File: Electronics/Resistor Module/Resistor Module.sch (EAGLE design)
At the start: 110 parts, among them IC1 74HC595D, IC2 74HC595D, IC3 74HC595D, IC4 74HC595D

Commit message: Updated schematic for full range module. 1/4 layout done.
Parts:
- removed $1_75_$: 25AA010A, Resistor Module Library:25AA010A
- removed JP3: (no value), Resistor Module Library:M03X2SMT-M0.1
- removed JP4: M10PASSTHROUGH, Resistor Module Library:M10PASSTHROUGH
- removed R33, R34, R35, R36, R37, R38, R39, R40: 2k, Resistor Module Library:RESISTOR0603-RES
- added R100: 10, Resistor Module Library:RESISTOR1206
- added R120: 1k, Resistor Module Library:RESISTOR1206
- added R160: 10k, Resistor Module Library:RESISTOR1206
- added R200: 100k, Resistor Module Library:RESISTOR1206
- added R240: 1M, Resistor Module Library:RESISTOR1206
- added R280: 10M, Resistor Module Library:RESISTOR1206
- added R320: 100M, Resistor Module Library:RESISTOR1206
- added R65, R66, R67, R68, R69, R70, R71, R72: 2k, Resistor Module Library:RESISTOR0603-RES
- added R73: 10k, Resistor Module Library:RESISTOR0603-RES
- added R80: 100, Resistor Module Library:RESISTOR1206
- added S29, S30, S31, S32: CPC1002N, Resistor Module Library:CPC1002N
- added U5: 25AA010A, Resistor Module Library:25AA010A
- JP2: value (none) -> M10PASSTHROUGH; device Resistor Module Library:M03X2969973-3 -> Resistor Module Library:M10PASSTHROUGH
- R25: value 10 -> 1M
- R26: value 100 -> 2M
- R27: value 1k -> 2M
- R28: value 10k -> 10M
- R29: value 100k -> 10M
- R30: value 1M -> 20M
- R31: value 2k -> 20M; device Resistor Module Library:RESISTOR0603-RES -> Resistor Module Library:RESISTOR1206
- R32: value 2k -> 100M; device Resistor Module Library:RESISTOR0603-RES -> Resistor Module Library:RESISTOR1206
- R59: value 10k -> 2k
- R60: value 1M -> 2k; device Resistor Module Library:RESISTOR1206 -> Resistor Module Library:RESISTOR0603-RES
- R61, R62: value 2M -> 2k; device Resistor Module Library:RESISTOR1206 -> Resistor Module Library:RESISTOR0603-RES
- R63, R64: value 10M -> 2k; device Resistor Module Library:RESISTOR1206 -> Resistor Module Library:RESISTOR0603-RES
- renumbered IC1 to U1, IC2 to U2, IC3 to U3, IC4 to U4
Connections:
- removed net N$40: R12.1, R13.2, R27.1, S12.DC-, S13.DC+
- removed net N$43: R16.1, R17.2, R28.1, S16.DC-, S17.DC+
- removed net N$9: R26.1, R8.1, R9.2, S8.DC-, S9.DC+
- removed net RELAY_POST_SHORT: R37.2, R51.2
- removed net RELAY_PRE_SHORT: R38.2, R52.2
- removed net R_DOWNSTREAM_IN: JP2.1
- removed net R_DOWNSTREAM_OUT: JP3.1
- removed net R_UPSTREAM: JP2.6, JP3.2
- removed net SERIAL_OUT: JP3.6
- new net N$53: R28.1, R280.1, R29.2, S28.DC-, S29.DC+
- new net N$58: R29.1, R30.2, S29.DC-, S30.DC+
- new net N$59: R30.1, R31.2, S30.DC-, S31.DC+
- new net N$60: R31.1, R32.2, R320.2, S31.DC-, S32.DC+
- new net N$61: R49.1, U2A.QA
- new net N$62: R57.1, U3A.QA
- new net N$64: R65.1, U4A.QA
- new net R120: R12.1, R120.1, R13.2, S12.DC-, S13.DC+
- new net R160: R16.1, R160.1, R17.2, S16.DC-, S17.DC+
- new net R80: R8.1, R80.1, R9.2, S8.DC-, S9.DC+
- new net RELAY_R29: R69.2, S29.C+
- new net RELAY_R30: R70.2, S30.C+
- new net RELAY_R31: R71.2, S31.C+
- new net RELAY_R32: R72.2, S32.C+
- new net R_OUT: JP2.2, R32.1, R320.1, S32.DC-
- net 5V: now also R73.2, U5.VDD; no longer $1_75_$.VDD, R59.2
- net 5V_2: now also JP2.6; no longer JP4.6
- net EEPROM_CS_L: now also JP1.1, R73.1, U5.CS; no longer $1_75_$.CS, R59.1, U1A.QA, U3A.QA
- net EEPROM_MISO: now also U5.SO; no longer $1_75_$.SO
- net EEPROM_MOSI: now also U5.SI; no longer $1_75_$.SI
- net EEPROM_SCK: now also U5.SCK; no longer $1_75_$.SCK
- net GND: now also S29.C-, S30.C-, S31.C-, S32.C-, U5.VSS; no longer $1_75_$.VSS
- net GND_2: now also JP2.5; no longer JP4.5
- net N$1: now also R48.1; no longer R37.1
- net N$12: now also R46.1; no longer R35.1
- net N$13: now also R45.1; no longer R34.1
- net N$14: now also R44.1; no longer R33.1
- net N$15: now also R120.2; no longer R27.2
- net N$16: now also R43.1; no longer R32.1
- net N$17: now also R42.1; no longer R31.1
- net N$18: now also R50.1; no longer R38.1
- net N$19: now also R51.1; no longer R39.1
- net N$2: now also R47.1; no longer R36.1
- net N$20: now also R52.1; no longer R40.1
- net N$21: now also R53.1; no longer R41.1
- net N$22: now also R54.1; no longer R42.1
- net N$23: now also R55.1; no longer R43.1
- net N$24: now also R56.1; no longer R44.1
- net N$26: now also R64.1; no longer R51.1
- net N$27: now also R63.1; no longer R50.1
- net N$28: now also R62.1; no longer R49.1
- net N$29: now also R61.1; no longer R48.1
- net N$30: now also R60.1; no longer R47.1
- net N$31: now also R59.1; no longer R46.1
- net N$32: now also R58.1; no longer R45.1
- net N$33: now also R66.1; no longer R52.1
- net N$34: now also R67.1; no longer R53.1
- net N$35: now also R68.1; no longer R54.1
- net N$36: now also R69.1; no longer R55.1
- net N$37: now also R70.1; no longer R56.1
- net N$38: now also R71.1; no longer R57.1
- net N$39: now also R72.1; no longer R58.1
- net N$4: now also R100.2; no longer R25.2
- net N$42: now also R160.2; no longer R28.2
- net N$46: now also R200.2; no longer R29.2
- net N$47: now also R200.1; no longer R29.1
- net N$5: now also R100.1; no longer R25.1
- net N$50: now also R240.2; no longer R30.2
- net N$52: now also R240.1, R25.2; no longer R30.1, R60.2
- net N$54: now also R25.1, R26.2; no longer R60.1, R61.2
- net N$55: now also R26.1, R27.2; no longer R61.1, R62.2
- net N$56: now also R27.1, R28.2, R280.2; no longer R62.1, R63.2, R64.2
- net N$57: now also R41.1, U1A.QA; no longer R63.1, R64.1, S28.DC-
- net N$8: now also R80.2; no longer R26.2
- net RELAY_R1: now also R41.2; no longer R36.2, R50.2
- net RELAY_R10: now also R50.2; no longer R41.2, R55.2
- net RELAY_R11: now also R51.2; no longer R40.2, R54.2
- net RELAY_R12: now also R52.2; no longer R39.2, R53.2
- net RELAY_R13: now also R53.2
- net RELAY_R14: now also R54.2
- net RELAY_R15: now also R55.2
- net RELAY_R16: now also R56.2
- net RELAY_R17: now also R57.2
- net RELAY_R18: now also R58.2
- net RELAY_R19: now also R59.2
- net RELAY_R2: now also R42.2; no longer R35.2, R49.2
- net RELAY_R20: now also R60.2
- net RELAY_R21: now also R61.2
- net RELAY_R22: now also R62.2
- net RELAY_R23: now also R63.2
- net RELAY_R24: now also R64.2
- net RELAY_R25: now also R65.2
- net RELAY_R26: now also R66.2
- net RELAY_R27: now also R67.2
- net RELAY_R28: now also R68.2
- net RELAY_R3: now also R43.2; no longer R34.2, R48.2
- net RELAY_R4: now also R44.2; no longer R33.2, R47.2
- net RELAY_R5: now also R45.2; no longer R32.2, R46.2
- net RELAY_R6: now also R46.2; no longer R31.2, R45.2
- net RELAY_R7: now also R47.2; no longer R44.2, R58.2
- net RELAY_R8: now also R48.2; no longer R43.2, R57.2
- net RELAY_R9: now also R49.2; no longer R42.2, R56.2
- net R_IN: now also JP2.1
- net SERIAL_CLK: now also JP1.8, U2A.SCK; no longer JP1.9, U3A.SCK
- net SERIAL_CLK_2: now also JP2.8, U3A.SCK; no longer JP4.9, U2A.SCK
- net SERIAL_IN: now also JP2.4; no longer JP2.2
- net SERIAL_LATCH: now also JP1.9, U2A.RCK; no longer JP1.8, U3A.RCK
- net SERIAL_LATCH_2: now also JP2.9, U3A.RCK; no longer JP4.8, U2A.RCK
- net SERIAL_MR_L: now also JP1.7, U2A.SCL; no longer JP1.10, U3A.SCL
- net SERIAL_MR_L_2: now also JP2.7, U3A.SCL; no longer JP4.10, U2A.SCL
- net SERIAL_OE_L: now also JP1.10, U2A.G; no longer JP1.7, U3A.G
- net SERIAL_OE_L_2: now also JP2.10, U3A.G; no longer JP4.7, U2A.G
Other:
- note removed: "BOTTOM"
- note removed: "TOP"
- moved on the sheet: C5, JP2, R25, R26, R27, R28, R29, R30, R41, R42, R43, R44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

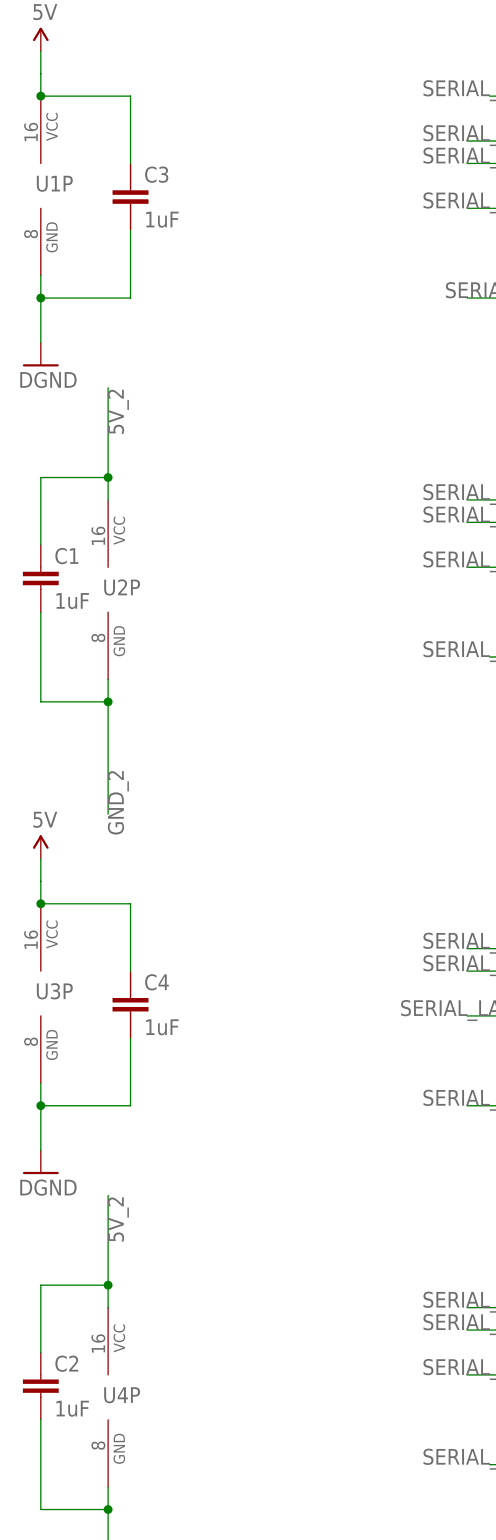
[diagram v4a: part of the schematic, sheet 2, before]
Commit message: Placed all relays and critical resistors.
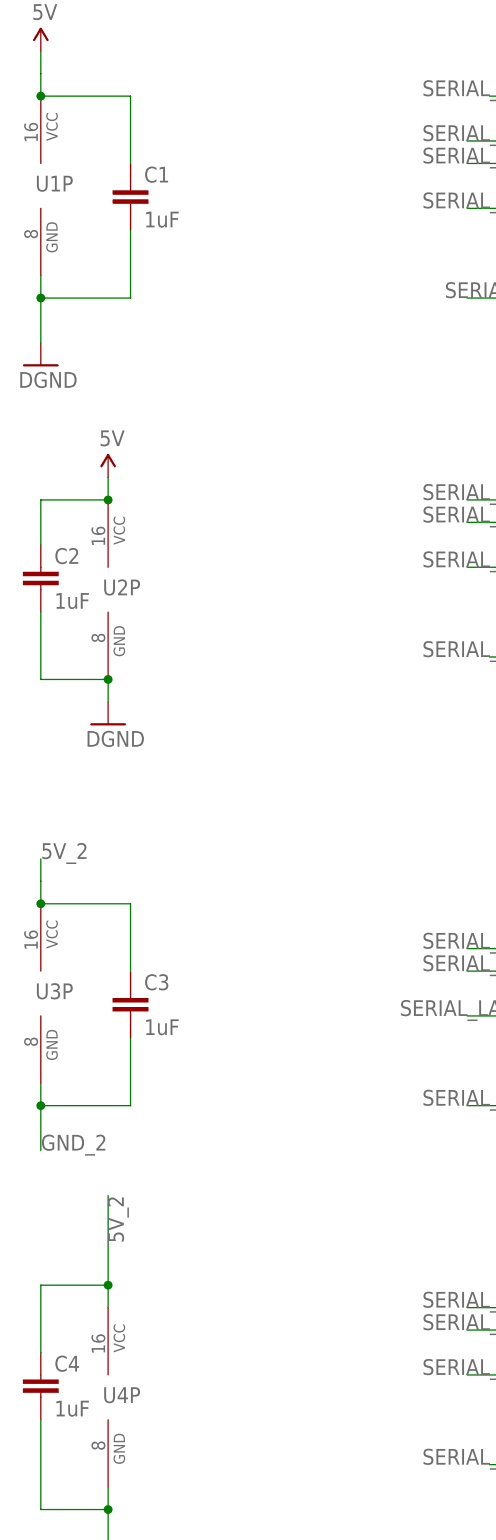
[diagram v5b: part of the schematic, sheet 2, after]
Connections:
- net 5V: now also C1.1, C2.1, U2P.VCC; no longer C3.1, C4.1, U3P.VCC
- net 5V_2: now also C3.1, C4.1, U3P.VCC; no longer C1.1, C2.1, U2P.VCC
- net GND: now also C1.2, C2.2, U2P.GND; no longer C3.2, C4.2, U3P.GND
- net GND_2: now also C3.2, C4.2, U3P.GND; no longer C1.2, C2.2, U2P.GND
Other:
- moved on the sheet: C1, C2, C3, C4
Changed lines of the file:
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@@
 <part name="SUPPLY6" library="Resistor Module Library" deviceset="5V" device=""/>
 <part name="GND19" library="Resistor Module Library" deviceset="DGND" device=""/>
-<part name="C3" library="Resistor Module Library" deviceset="CAP" device="0603-CAP" value="1uF"/>
 <part name="C1" library="Resistor Module Library" deviceset="CAP" device="0603-CAP" value="1uF"/>
+<part name="C2" library="Resistor Module Library" deviceset="CAP" device="0603-CAP" value="1uF"/>
 <part name="C5" library="Resistor Module Library" deviceset="CAP" device="0603-CAP" value="1uF"/>
 <part name="GND2" library="Resistor Module Library" deviceset="DGND" device=""/>
 <part name="U3" library="Resistor Module Library" deviceset="74*595" device="D" technology="HC" value="74HC595D"/>
 <part name="U4" library="Resistor Module Library" deviceset="74*595" device="D" technology="HC" value="74HC595D"/>
-<part name="SUPPLY2" library="Resistor Module Library" deviceset="5V" device=""/>
-<part name="GND9" library="Resistor Module Library" deviceset="DGND" device=""/>
 <part name="R66" library="Resistor Module Library" deviceset="RESISTOR" device="0603-RES" value="2k"/>
 <part name="R63" library="Resistor Module Library" deviceset="RESISTOR" device="0603-RES" value="2k"/>
@@
 <part name="R67" library="Resistor Module Library" deviceset="RESISTOR" device="0603-RES" value="2k"/>
 <part name="R64" library="Resistor Module Library" deviceset="RESISTOR" device="0603-RES" value="2k"/>
+<part name="C3" library="Resistor Module Library" deviceset="CAP" device="0603-CAP" value="1uF"/>
 <part name="C4" library="Resistor Module Library" deviceset="CAP" device="0603-CAP" value="1uF"/>
-<part name="C2" library="Resistor Module Library" deviceset="CAP" device="0603-CAP" value="1uF"/>
 <part name="GND10" library="Resistor Module Library" deviceset="DGND" device=""/>
 <part name="GND11" library="Resistor Module Library" deviceset="DGND" device=""/>
@@
 <part name="R65" library="Resistor Module Library" deviceset="RESISTOR" device="0603-RES" value="2k"/>
 <part name="R57" library="Resistor Module Library" deviceset="RESISTOR" device="0603-RES" value="2k"/>
+<part name="GND9" library="Resistor Module Library" deviceset="DGND" device=""/>
+<part name="SUPPLY2" library="Resistor Module Library" deviceset="5V" device=""/>
 </parts>
 <sheets>
@@
 </instance>
 <instance part="SUPPLY4" gate="G$1" x="35.56" y="-96.52"/>
-<instance part="C3" gate="G$1" x="-66.04" y="71.12"/>
-<instance part="C1" gate="G$1" x="-76.2" y="27.94"/>
+<instance part="C1" gate="G$1" x="-66.04" y="71.12"/>
+<instance part="C2" gate="G$1" x="-76.2" y="27.94"/>
 <instance part="C5" gate="G$1" x="0" y="-104.14" rot="R90"/>
 <instance part="GND2" gate="G$1" x="-15.24" y="-109.22"/>
@@
 <instance part="U3" gate="P" x="-76.2" y="-17.78"/>
 <instance part="U4" gate="P" x="-68.58" y="-63.5"/>
-<instance part="SUPPLY2" gate="G$1" x="-76.2" y="-2.54"/>
-<instance part="GND9" gate="G$1" x="-76.2" y="-38.1"/>
 <instance part="R66" gate="G$1" x="20.32" y="-50.8" smashed="yes">
 <attribute name="NAME" x="11.43" y="-50.5714" size="1.778" layer="95"/>
@@
 <attribute name="VALUE" x="25.4" y="-24.892" size="1.778" layer="96"/>
 </instance>
-<instance part="C4" gate="G$1" x="-66.04" y="-20.32"/>
-<instance part="C2" gate="G$1" x="-76.2" y="-63.5"/>
+<instance part="C3" gate="G$1" x="-66.04" y="-20.32"/>
+<instance part="C4" gate="G$1" x="-76.2" y="-63.5"/>
 <instance part="R41" gate="G$1" x="20.32" y="83.82" smashed="yes">
 <attribute name="NAME" x="11.43" y="84.0486" size="1.778" layer="95"/>
@@
 <attribute name="VALUE" x="25.4" y="-7.112" size="1.778" layer="96"/>
 </instance>
+<instance part="GND9" gate="G$1" x="-68.58" y="12.7"/>
+<instance part="SUPPLY2" gate="G$1" x="-68.58" y="40.64"/>
 </instances>
 <busses>
@@
 <wire x1="-76.2" y1="83.82" x2="-76.2" y2="86.36" width="0.1524" layer="91"/>
 <wire x1="-76.2" y1="86.36" x2="-76.2" y2="88.9" width="0.1524" layer="91"/>
-<pinref part="C3" gate="G$1" pin="1"/>
+<pinref part="C1" gate="G$1" pin="1"/>
 <wire x1="-66.04" y1="76.2" x2="-66.04" y2="83.82" width="0.1524" layer="91"/>
 <wire x1="-66.04" y1="83.82" x2="-76.2" y2="83.82" width="0.1524" layer="91"/>
@@
 </segment>
 <segment>
-<pinref part="U3" gate="P" pin="VCC"/>
 <pinref part="SUPPLY2" gate="G$1" pin="5V"/>
-<wire x1="-76.2" y1="-7.62" x2="-76.2" y2="-5.08" width="0.1524" layer="91"/>
-<wire x1="-76.2" y1="-5.08" x2="-76.2" y2="-2.54" width="0.1524" layer="91"/>
-<pinref part="C4" gate="G$1" pin="1"/>
-<wire x1="-66.04" y1="-15.24" x2="-66.04" y2="-7.62" width="0.1524" layer="91"/>
-<wire x1="-66.04" y1="-7.62" x2="-76.2" y2="-7.62" width="0.1524" layer="91"/>
-<junction x="-76.2" y="-7.62"/>
+<pinref part="U2" gate="P" pin="VCC"/>
+<wire x1="-68.58" y1="40.64" x2="-68.58" y2="38.1" width="0.1524" layer="91"/>
+<pinref part="C2" gate="G$1" pin="1"/>
+<wire x1="-76.2" y1="33.02" x2="-76.2" y2="38.1" width="0.1524" layer="91"/>
+<wire x1="-76.2" y1="38.1" x2="-68.58" y2="38.1" width="0.1524" layer="91"/>
+<junction x="-68.58" y="38.1"/>
 </segment>
 </net>
@@
 <pinref part="U1" gate="P" pin="GND"/>
 <wire x1="-76.2" y1="55.88" x2="-76.2" y2="60.96" width="0.1524" layer="91"/>
-<pinref part="C3" gate="G$1" pin="2"/>
+<pinref part="C1" gate="G$1" pin="2"/>
 <wire x1="-76.2" y1="60.96" x2="-76.2" y2="63.5" width="0.1524" layer="91"/>
 <wire x1="-66.04" y1="68.58" x2="-66.04" y2="60.96" width="0.1524" layer="91"/>
@@
 </segment>
 <segment>
+<pinref part="C2" gate="G$1" pin="2"/>
+<wire x1="-76.2" y1="25.4" x2="-76.2" y2="17.78" width="0.1524" layer="91"/>
+<pinref part="U2" gate="P" pin="GND"/>
+<wire x1="-76.2" y1="17.78" x2="-68.58" y2="17.78" width="0.1524" layer="91"/>
 <pinref part="GND9" gate="G$1" pin="GND"/>
-<pinref part="U3" gate="P" pin="GND"/>
-<wire x1="-76.2" y1="-35.56" x2="-76.2" y2="-30.48" width="0.1524" layer="91"/>
-<pinref part="C4" gate="G$1" pin="2"/>
-<wire x1="-76.2" y1="-30.48" x2="-76.2" y2="-27.94" width="0.1524" layer="91"/>
-<wire x1="-66.04" y1="-22.86" x2="-66.04" y2="-30.48" width="0.1524" layer="91"/>
-<wire x1="-66.04" y1="-30.48" x2="-76.2" y2="-30.48" width="0.1524" layer="91"/>
-<junction x="-76.2" y="-30.48"/>
+<wire x1="-68.58" y1="17.78" x2="-68.58" y2="15.24" width="0.1524" layer="91"/>
+<junction x="-68.58" y="17.78"/>
 </segment>
 </net>
@@
 <net name="5V_2" class="0">
 <segment>
-<pinref part="U2" gate="P" pin="VCC"/>
-<wire x1="-68.58" y1="38.1" x2="-68.58" y2="40.64" width="0.1524" layer="91"/>
-<label x="-68.58" y="50.8" size="1.778" layer="95" rot="R270"/>
-<pinref part="C1" gate="G$1" pin="1"/>
-<wire x1="-68.58" y1="40.64" x2="-68.58" y2="50.8" width="0.1524" layer="91"/>
-<wire x1="-76.2" y1="33.02" x2="-76.2" y2="40.64" width="0.1524" layer="91"/>
-<wire x1="-76.2" y1="40.64" x2="-68.58" y2="40.64" width="0.1524" layer="91"/>
-<junction x="-68.58" y="40.64"/>
-</segment>
-<segment>
 <pinref part="U4" gate="P" pin="VCC"/>
 <wire x1="-68.58" y1="-53.34" x2="-68.58" y2="-50.8" width="0.1524" layer="91"/>
 <label x="-68.58" y="-40.64" size="1.778" layer="95" rot="R270"/>
-<pinref part="C2" gate="G$1" pin="1"/>
+<pinref part="C4" gate="G$1" pin="1"/>
 <wire x1="-68.58" y1="-50.8" x2="-68.58" y2="-40.64" width="0.1524" layer="91"/>
 <wire x1="-76.2" y1="-58.42" x2="-76.2" y2="-50.8" width="0.1524" layer="91"/>
@@
 <junction x="-68.58" y="-50.8"/>
 </segment>
+<segment>
+<pinref part="U3" gate="P" pin="VCC"/>
+<wire x1="-76.2" y1="-7.62" x2="-76.2" y2="-5.08" width="0.1524" layer="91"/>
+<wire x1="-76.2" y1="-5.08" x2="-76.2" y2="-2.54" width="0.1524" layer="91"/>
+<pinref part="C3" gate="G$1" pin="1"/>
+<wire x1="-66.04" y1="-15.24" x2="-66.04" y2="-7.62" width="0.1524" layer="91"/>
+<wire x1="-66.04" y1="-7.62" x2="-76.2" y2="-7.62" width="0.1524" layer="91"/>
+<junction x="-76.2" y="-7.62"/>
+<label x="-76.2" y="-2.54" size="1.778" layer="95"/>
+</segment>
 </net>
 <net name="GND_2" class="0">
-<segment>
-<pinref part="U2" gate="P" pin="GND"/>
-<wire x1="-68.58" y1="17.78" x2="-68.58" y2="15.24" width="0.1524" layer="91"/>
-<label x="-68.58" y="7.62" size="1.778" layer="95" rot="R270"/>
-<pinref part="C1" gate="G$1" pin="2"/>
-<wire x1="-68.58" y1="15.24" x2="-68.58" y2="2.54" width="0.1524" layer="91"/>
-<wire x1="-76.2" y1="25.4" x2="-76.2" y2="15.24" width="0.1524" layer="91"/>
-<wire x1="-76.2" y1="15.24" x2="-68.58" y2="15.24" width="0.1524" layer="91"/>
-<junction x="-68.58" y="15.24"/>
-</segment>
 <segment>
 <pinref part="U4" gate="P" pin="GND"/>
 <wire x1="-68.58" y1="-73.66" x2="-68.58" y2="-76.2" width="0.1524" layer="91"/>
 <label x="-68.58" y="-83.82" size="1.778" layer="95" rot="R270"/>
-<pinref part="C2" gate="G$1" pin="2"/>
+<pinref part="C4" gate="G$1" pin="2"/>
 <wire x1="-68.58" y1="-76.2" x2="-68.58" y2="-88.9" width="0.1524" layer="91"/>
 <wire x1="-76.2" y1="-66.04" x2="-76.2" y2="-76.2" width="0.1524" layer="91"/>
 <wire x1="-76.2" y1="-76.2" x2="-68.58" y2="-76.2" width="0.1524" layer="91"/>
 <junction x="-68.58" y="-76.2"/>
+</segment>
+<segment>
+<pinref part="U3" gate="P" pin="GND"/>
+<wire x1="-76.2" y1="-35.56" x2="-76.2" y2="-30.48" width="0.1524" layer="91"/>
+<pinref part="C3" gate="G$1" pin="2"/>
+<wire x1="-76.2" y1="-30.48" x2="-76.2" y2="-27.94" width="0.1524" layer="91"/>
+<wire x1="-66.04" y1="-22.86" x2="-66.04" y2="-30.48" width="0.1524" layer="91"/>
+<wire x1="-66.04" y1="-30.48" x2="-76.2" y2="-30.48" width="0.1524" layer="91"/>
+<junction x="-76.2" y="-30.48"/>
+<label x="-76.2" y="-35.56" size="1.778" layer="95"/>
 </segment>
 </net>
@@
 </sheet>
 </sheets>
-<errors>
-</errors>
 </schematic>
 </drawing>
